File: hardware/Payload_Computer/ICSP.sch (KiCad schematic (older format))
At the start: 3 parts

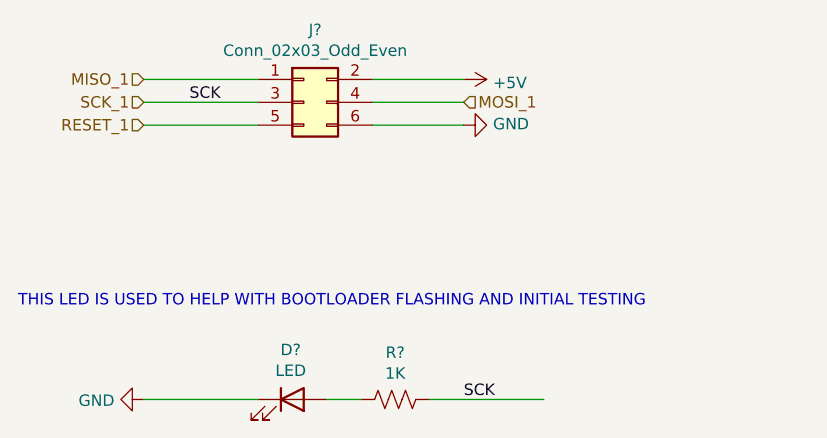
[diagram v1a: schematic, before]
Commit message: Finished BNO055
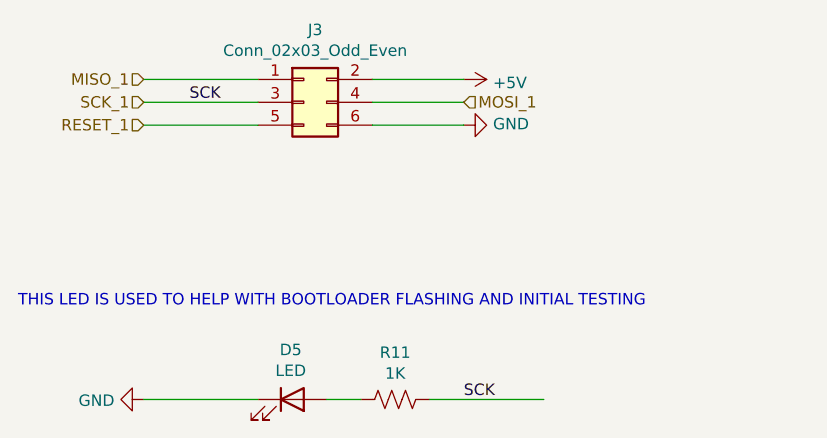
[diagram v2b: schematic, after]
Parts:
- gave numbers to parts that had none: 3
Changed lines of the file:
@@
 $Descr A4 11693 8268
 encoding utf-8
-Sheet 10 17
+Sheet 10 15
 Title ""
 Date ""
@@
 $EndDescr
 $Comp
-L Connector_Generic:Conn_02x03_Odd_Even J?
+L Connector_Generic:Conn_02x03_Odd_Even J3
 U 1 1 5F8F15C1
 P 5900 3950
-F 0 "J?" H 5950 4267 50  0000 C CNN
+F 0 "J3" H 5950 4267 50  0000 C CNN
 F 1 "Conn_02x03_Odd_Even" H 5950 4176 50  0000 C CNN
 F 2 "" H 5900 3950 50  0001 C CNN
@@
 RESET_1
 $Comp
-L Device:LED D?
+L Device:LED D5
 U 1 1 5F985B10
 P 5850 5250
-F 0 "D?" H 5843 5467 50  0000 C CNN
+F 0 "D5" H 5843 5467 50  0000 C CNN
 F 1 "LED" H 5843 5376 50  0000 C CNN
 F 2 "" H 5850 5250 50  0001 C CNN
@@
 $EndComp
 $Comp
-L Device:R_US R?
+L Device:R_US R11
 U 1 1 5F9867EE
 P 6300 5250
-F 0 "R?" V 6095 5250 50  0000 C CNN
+F 0 "R11" V 6095 5250 50  0000 C CNN
 F 1 "1K" V 6186 5250 50  0000 C CNN
 F 2 "" V 6340 5240 50  0001 C CNN
@@
 $EndComp
 $Comp
-L power:GND #PWR?
+L power:GND #PWR0137
 U 1 1 5F986F6F
 P 5200 5250
-F 0 "#PWR?" H 5200 5000 50  0001 C CNN
+F 0 "#PWR0137" H 5200 5000 50  0001 C CNN
 F 1 "GND" V 5205 5122 50  0000 R CNN
 F 2 "" H 5200 5250 50  0001 C CNN
